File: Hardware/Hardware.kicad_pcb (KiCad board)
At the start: 2 copper layers, 60 x 40 mm, 52 parts, among them J1 Serial Wire Debug(SWD), J2 Conn_01x07 USART2, J3 Conn_01x07 LPUART1, J4 Conn_01x08 SPI1, J5 Conn_01x05 I2C, Q1 Q_NPN_BEC BSR17A, Q2 BC547, Q3 BC547, U1 Opamp_Quad, U4 TLV74115_SOT23-5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

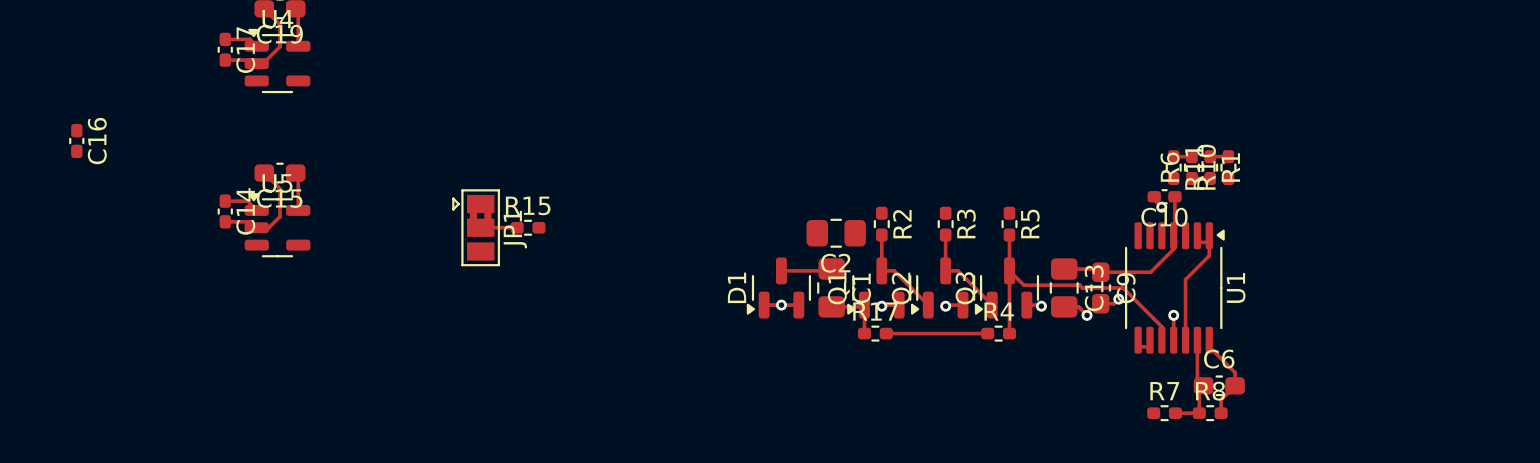
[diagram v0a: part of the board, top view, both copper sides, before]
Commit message: added more footprints and continued on the circuit diagram
- [ ] add antenna connection
- [ ] find suitable 390Mohm resistor
- [ ] add switches, reset and power
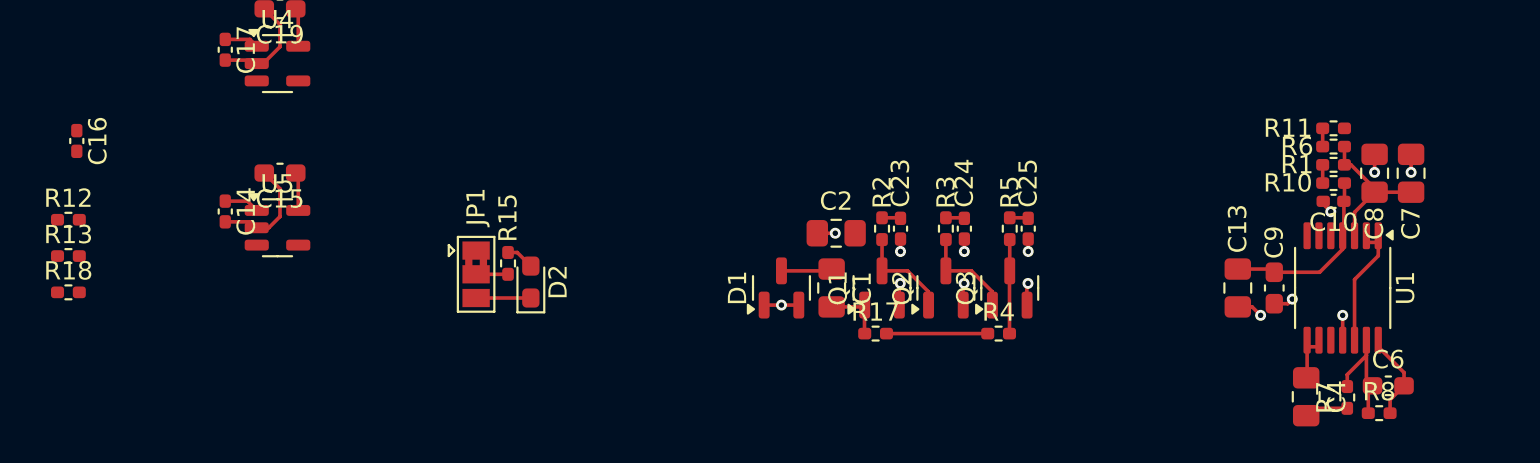
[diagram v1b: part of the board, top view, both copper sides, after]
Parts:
- added C23: 100nF, Capacitor_SMD:C_0402_1005Metric_Pad0.74x0.62mm_HandSolder, F.Cu at (61.8, 81.8)
- added C24: 100nF, Capacitor_SMD:C_0402_1005Metric_Pad0.74x0.62mm_HandSolder, F.Cu at (65.3, 81.8)
- added C25: 100nF, Capacitor_SMD:C_0402_1005Metric_Pad0.74x0.62mm_HandSolder, F.Cu at (68.8, 81.8)
- added C4: 1uF, Capacitor_SMD:C_0805_2012Metric_Pad1.18x1.45mm_HandSolder, F.Cu at (84.0, 91.0)
- added C7: 1uF, Capacitor_SMD:C_0805_2012Metric_Pad1.18x1.45mm_HandSolder, F.Cu at (89.8, 78.7)
- added C8: 1uF, Capacitor_SMD:C_0805_2012Metric_Pad1.18x1.45mm_HandSolder, F.Cu at (87.8, 78.7)
- added D2: LED BLUE, IF≈1mA@2.6V, APT1608LVBx, LED_SMD:LED_0603_1608Metric_Pad1.05x0.95mm_HandSolder, F.Cu at (41.5, 84.7)
- added R12: 2MΩ, Resistor_SMD:R_0402_1005Metric_Pad0.72x0.64mm_HandSolder, F.Cu at (16.2, 81.3)
- added R13: 39MΩ, Resistor_SMD:R_0402_1005Metric_Pad0.72x0.64mm_HandSolder, F.Cu at (16.2, 83.2)
- added R18: 2MΩ, Resistor_SMD:R_0402_1005Metric_Pad0.72x0.64mm_HandSolder, F.Cu at (16.2, 85.2)
- moved R7 10.0 mm to (86.2, 91.0), turned to 90 degrees
- moved C13 9.51 mm to (80.2, 85.0)
- moved C9 9.51 mm to (82.2, 85.0)
- moved C10 9.27 mm to (85.5, 80.2)
- moved C6 9.26 mm to (88.5, 90.4)
- moved R8 9.26 mm to (88.0, 91.9)
- moved U1 9.26 mm to (86.0, 85.0)
- moved R11 9.02 mm to (85.5, 76.2), turned to 0 degrees
- moved R6 7.85 mm to (85.5, 77.2), turned to 180 degrees
- moved R1 6.76 mm to (85.5, 78.2), turned to 0 degrees
- moved R10 5.82 mm to (85.5, 79.2), turned to 180 degrees
- moved JP1 2.56 mm to (38.5, 84.2)
- moved R15 2.24 mm to (40.2, 83.7), turned to 90 degrees
- moved R2 0.25 mm to (60.8, 81.8)
- moved R3 0.25 mm to (64.2, 81.8)
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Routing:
- net /Original Smog Detector/Output DC-Coupled: track 15.8 -> 5.15 mm
- net GND: track 24.8 -> 33.6 mm, vias 8 -> 14
- net Net-(U1A-+): track 1.00 -> 8.24 mm
- net +1V5: track 2.11 -> 5.18 mm
- net Net-(C4-Pad2): track 0.00 -> 2.42 mm
- net Net-(U1C--): track 0.65 -> 2.73 mm
- net Net-(D2-A): track 0.00 -> 1.56 mm
- net Net-(U1D--): track 5.18 -> 6.37 mm
- net +3V3: track 22.4 -> 22.9 mm

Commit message: PCB is done???
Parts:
- removed J3: Conn_01x07 LPUART1, Connector_PinHeader_2.54mm:PinHeader_1x07_P2.54mm_Vertical
- removed J4: Conn_01x08 SPI1, Connector_PinHeader_2.54mm:PinHeader_1x08_P2.54mm_Vertical
- removed J5: Conn_01x05 I2C, Connector_PinHeader_2.54mm:PinHeader_1x05_P2.54mm_Vertical
- removed JP10, JP2, JP3, JP4, JP5, JP6, JP7, JP8, JP9: SolderJumper_3_Open, Jumper:SolderJumper-3_P1.3mm_Open_Pad1.0x1.5mm
- added AE1: Antenna_Shield, Connector_PinHeader_2.54mm:PinHeader_1x02_P2.54mm_Vertical_SMD_Pin1Left, F.Cu at (74.8, 54.5)
- added C3: C_Polarized 10µF 16V, Capacitor_SMD:C_0805_2012Metric_Pad1.18x1.45mm_HandSolder, F.Cu at (61.9, 44.5)
- added C5: 150nF, Capacitor_SMD:C_0402_1005Metric_Pad0.74x0.62mm_HandSolder, F.Cu at (40.7, 31.2)
- added R14: 330MΩ preferably 390MΩ, Resistor_SMD:R_0603_1608Metric_Pad0.98x0.95mm_HandSolder, F.Cu at (31.2, 58.8)
- added SW1: Power_Hard, Button_Switch_SMD:SW_SPDT_PCM12, F.Cu at (22.3, 45.0)
- added SW2: Power_Soft, Button_Switch_SMD:SW_SPDT_PCM12, F.Cu at (22.3, 54.5)
- added SW3: Reset, Button_Switch_SMD:SW_Push_1P1T_NO_6x6mm_H9.5mm, F.Cu at (75.8, 26.0)
- J1: value Serial Wire Debug(SWD) -> SWD
- J2: footprint Connector_PinHeader_2.54mm:PinHeader_1x07_P2.54mm_Vertical -> Connector_PinHeader_2.54mm:PinHeader_1x07_P2.54mm_Vertical_SMD_Pin1Left
- moved J1 81.8 mm to (22.2, 22.2)
- moved C21 69.8 mm to (31.2, 34.2)
- moved J2 69.1 mm to (40.5, 39.8), turned to -90 degrees
- moved C18 63.8 mm to (32.5, 23.2), turned to 0 degrees
- moved C20 62.1 mm to (32.5, 24.8), turned to 0 degrees
- moved JP1 61.6 mm to (41.0, 22.8), turned to 0 degrees
- moved R8 60.9 mm to (68.9, 34.0), turned to 90 degrees
- moved C6 60.7 mm to (67.4, 33.5), turned to 90 degrees
- moved R15 59.2 mm to (40.4, 24.5), turned to 180 degrees
- moved D2 58.9 mm to (41.4, 25.8), turned to 180 degrees
- moved R7 58.2 mm to (68.0, 35.8), turned to 180 degrees
- moved C7 57.6 mm to (55.7, 32.2), turned to 180 degrees
- moved U6 57.1 mm to (32.5, 29.2), turned to 90 degrees
- moved C4 55.3 mm to (68.0, 38.0), turned to 0 degrees
- moved C8 54.8 mm to (55.7, 34.2), turned to 180 degrees
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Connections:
- J2 pad 2: /MCU/USART2_TX -> /MCU/PA2 A2
- J2 pad 3: /MCU/USART2_RX -> /MCU/PA3 A3
- J2 pad 4: /MCU/USART2_RTS -> /MCU/PA1 A1
- J2 pad 5: /MCU/USART2_CTS -> /MCU/PA0 A0
- J2 pad 6: /MCU/USART2_CK -> /MCU/PA4 A4
- R9 pad 2: /MCU/IN Signal -> /MCU/PA5 A5
- U1 pad 1: /MCU/IN Ref -> /MCU/PA6 A6
- U1 pad 12: /MCU/IN Ref -> /MCU/PA6 A6
- U1 pad 2: /MCU/IN Ref -> /MCU/PA6 A6
- U1 pad 5: unconnected-(U1B-+-Pad5) -> GND
- U1 pad 6: unconnected-(U1B---Pad6) -> +3V3
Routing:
- net +3V3: track 22.9 -> 104.6 mm
- net /MCU/NRST: track 0.00 -> 68.4 mm, vias 0 -> 4
- net /PSU/+BATT_SWITCH: track 3.82 -> 55.3 mm, vias 0 -> 6
- net /MCU/PA6 A6: track 0.00 -> 43.4 mm, vias 0 -> 2
- net /MCU/IN Ref: track 34.9 -> 0.00 mm, vias 3 -> 0
- net Net-(C6-Pad2): track 4.54 -> 34.4 mm
- net +1V5: track 5.18 -> 34.5 mm
- net /MCU/IN Signal: track 28.0 -> 0.00 mm, vias 3 -> 0
- net /Original Smog Detector/Output DC-Coupled: track 5.15 -> 28.3 mm
- net /PSU/EN: track 0.00 -> 19.4 mm
- net GND: track 33.6 -> 51.2 mm, vias 14 -> 30
- net /MCU/PA2 A2: track 0.00 -> 17.2 mm, vias 0 -> 2
- net /MCU/PA1 A1: track 0.00 -> 14.1 mm, vias 0 -> 2
- net /MCU/PA4 A4: track 0.00 -> 13.2 mm, vias 0 -> 2
- net /MCU/PA5 A5: track 0.00 -> 12.3 mm, vias 0 -> 2
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- added copper zone on B.Cu, net GND
- removed copper zone on F.Cu, net GND
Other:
- board text added: "+3V3"
- board text added: "Boot0"
- board text added: "GND"
- board text added: "NRST"
- board text added: "SWCLK"
- board text added: "SWDIO"

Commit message: added headphone jack footprint, SJ-3524-SMT
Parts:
- added C26: 10uF, Capacitor_SMD:C_0805_2012Metric_Pad1.18x1.45mm_HandSolder, F.Cu at (82.2, 46.5)
- added J6: AudioJack3_SwitchT, Connector_Audio:Jack_3.5mm_CUI_SJ-3524-SMT_Horizontal, F.Cu at (89.2, 39.7)
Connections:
- C6 pad 1: Net-(U1D--) -> Net-(U1D-+)
- C6 pad 2: Net-(C6-Pad2) -> Net-(U1B-+)
- R7 pad 2: Net-(U1D--) -> Net-(U1D-+)
- R8 pad 1: Net-(U1D--) -> Net-(U1D-+)
- R8 pad 2: Net-(C6-Pad2) -> Net-(U1B-+)
- R9 pad 1: Net-(C6-Pad2) -> Net-(U1B-+)
- U1 pad 12: /MCU/PA6 A6 -> Net-(U1D-+)
- U1 pad 13: Net-(U1D--) -> /MCU/PA6 A6
- U1 pad 14: Net-(C6-Pad2) -> Net-(U1B-+)
- U1 pad 5: GND -> Net-(U1B-+)
- U1 pad 6: +3V3 -> Net-(U1B--)
- U1 pad 7: unconnected-(U1-Pad7) -> Net-(U1B--)
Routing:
- net Net-(U1B-+): track 0.00 -> 34.4 mm
- net Net-(C6-Pad2): track 34.4 -> 0.00 mm
- net /MCU/PA6 A6: track 43.4 -> 49.7 mm
- net Net-(U1D--): track 6.37 -> 0.00 mm

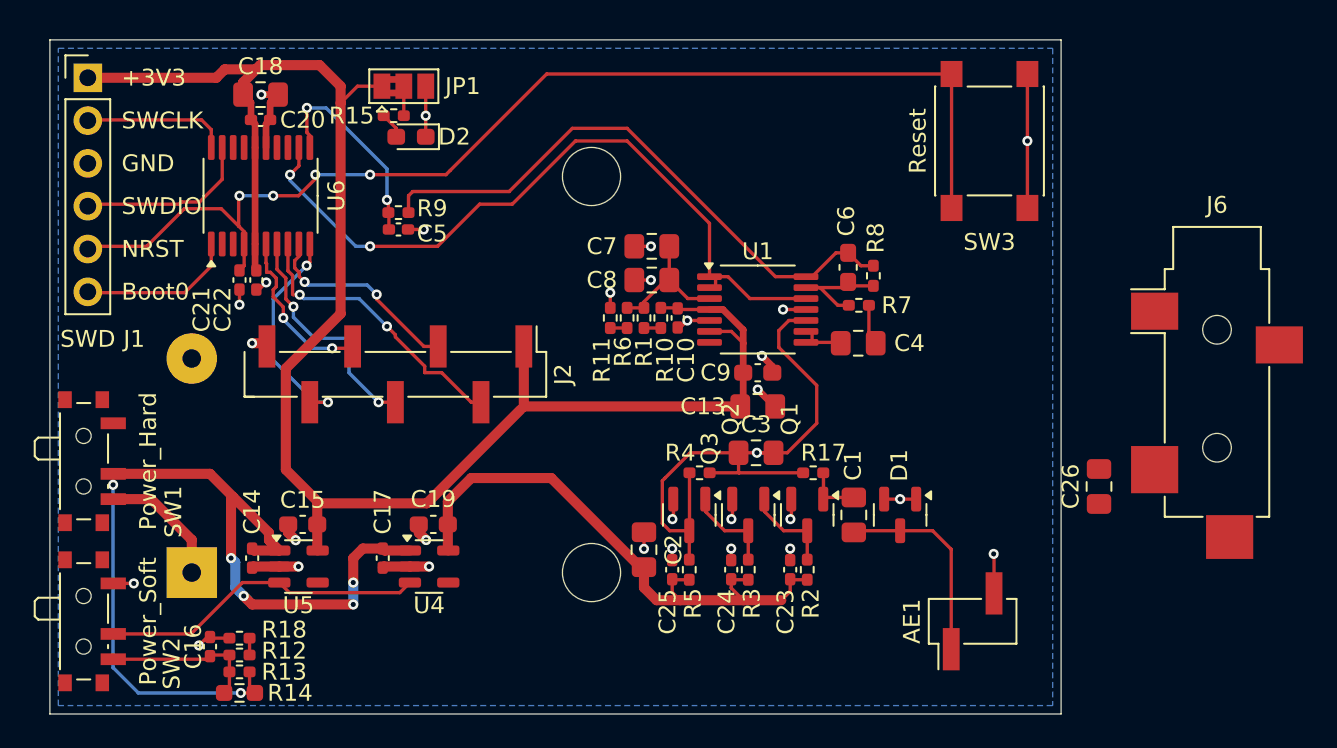
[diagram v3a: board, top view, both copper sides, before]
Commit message: PCB layed-out
- [x] headphone jack
- [x] UART header
- [x] Only one power trace with sub optimal return path
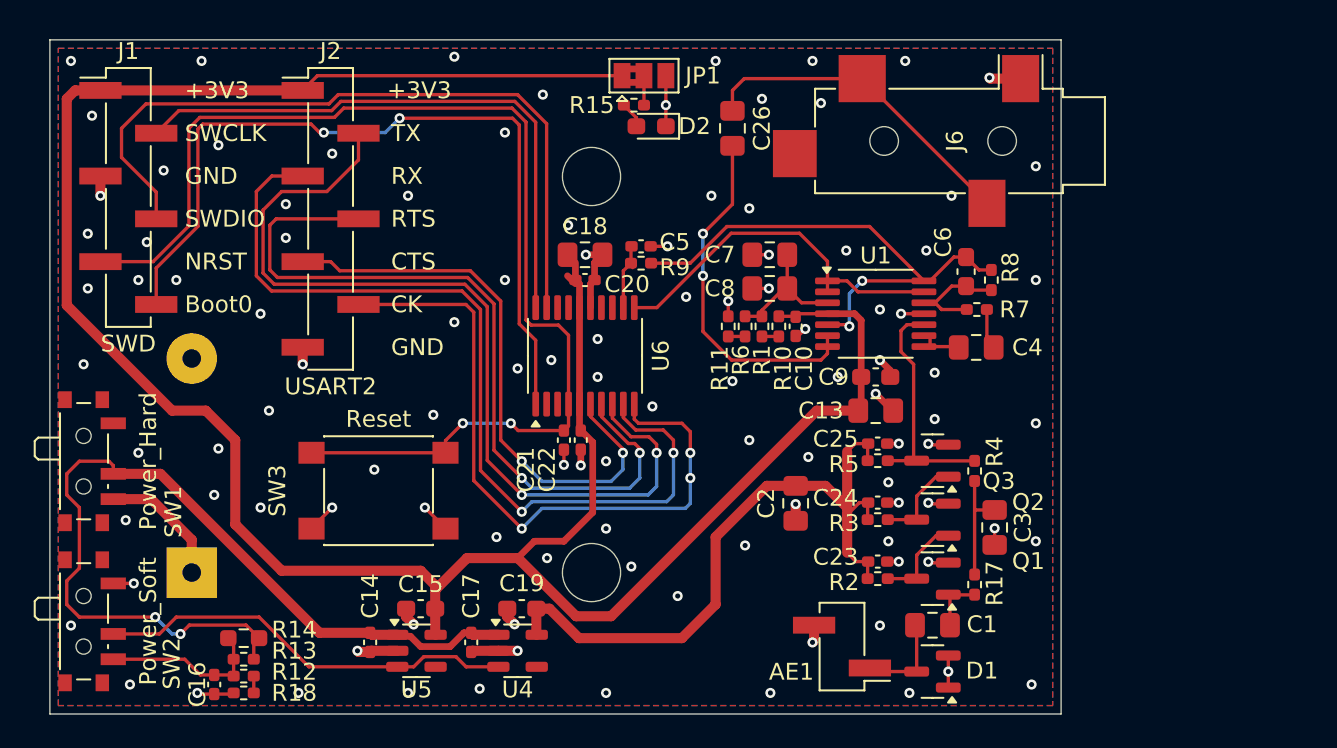
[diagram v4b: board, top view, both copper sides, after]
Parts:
- J1: footprint Connector_PinHeader_2.54mm:PinHeader_1x06_P2.54mm_Vertical -> Connector_PinHeader_2.54mm:PinHeader_1x06_P2.54mm_Vertical_SMD_Pin1Left
- J2: value Conn_01x07 USART2 -> USART2
- moved SW3 41.8 mm to (39.5, 46.8), turned to 180 degrees
- moved C26 30.4 mm to (60.5, 25.2)
- moved C18 21.5 mm to (51.8, 32.8)
- moved C20 21.5 mm to (51.8, 34.2)
- moved C21 21.5 mm to (50.5, 43.8)
- moved C22 21.5 mm to (51.5, 43.8)
- moved U6 21.5 mm to (51.8, 38.8)
- moved J6 20.5 mm to (74.0, 26.0), turned to -90 degrees
- moved R4 16.3 mm to (74.9, 45.6), turned to 90 degrees
- moved C3 14.8 mm to (76.1, 48.9), turned to -90 degrees
- moved Q3 14.8 mm to (72.4, 45.0), turned to 180 degrees
- moved R9 14.7 mm to (55.1, 33.2)
- moved C5 14.4 mm to (55.1, 32.2)
- moved C25 14.3 mm to (69.1, 44.0), turned to 0 degrees
- moved D2 14.3 mm to (55.7, 25.1)
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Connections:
- C5 pad 1: /MCU/PA5 A5 -> /MCU/PA6 A6
- R9 pad 2: /MCU/PA5 A5 -> /MCU/PA6 A6
- U1 pad 1: /MCU/PA6 A6 -> /MCU/PA5 A5
- U1 pad 13: /MCU/PA6 A6 -> /MCU/PA5 A5
- U1 pad 2: /MCU/PA6 A6 -> /MCU/PA5 A5
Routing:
- net /MCU/PA6 A6: track 49.7 -> 3.88 mm, vias 2 -> 0
- net +3V3: track 104.6 -> 145.2 mm
- net /MCU/PA3 A3: track 12.3 -> 52.3 mm
- net /MCU/PB9 Boot0: track 9.31 -> 48.3 mm, vias 0 -> 2
- net /MCU/PA2 A2: track 17.2 -> 53.2 mm
- net /MCU/PA13 SWDIO: track 10.5 -> 43.9 mm
- net /MCU/PA1 A1: track 14.1 -> 46.3 mm
- net /MCU/PA4 A4: track 13.2 -> 40.4 mm, vias 2 -> 3
- net /MCU/PA14 SWCLK: track 8.64 -> 34.8 mm
- net /MCU/PA0 A0: track 10.1 -> 34.2 mm
- net Net-(U1B--): track 0.00 -> 21.1 mm, vias 0 -> 2
- net Net-(C26-Pad2): track 0.00 -> 19.7 mm
- net /Original Smog Detector/Output DC-Coupled: track 28.3 -> 14.8 mm
- net /MCU/PA5 A5: track 12.3 -> 21.8 mm, vias 2 -> 0
- net Net-(U1D-+): track 0.00 -> 6.57 mm
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- added copper zone on F.Cu, net GND
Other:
- board text added: "CK"
- board text added: "CTS"
- board text added: "RTS"
- board text added: "RX"
- board text added: "TX"

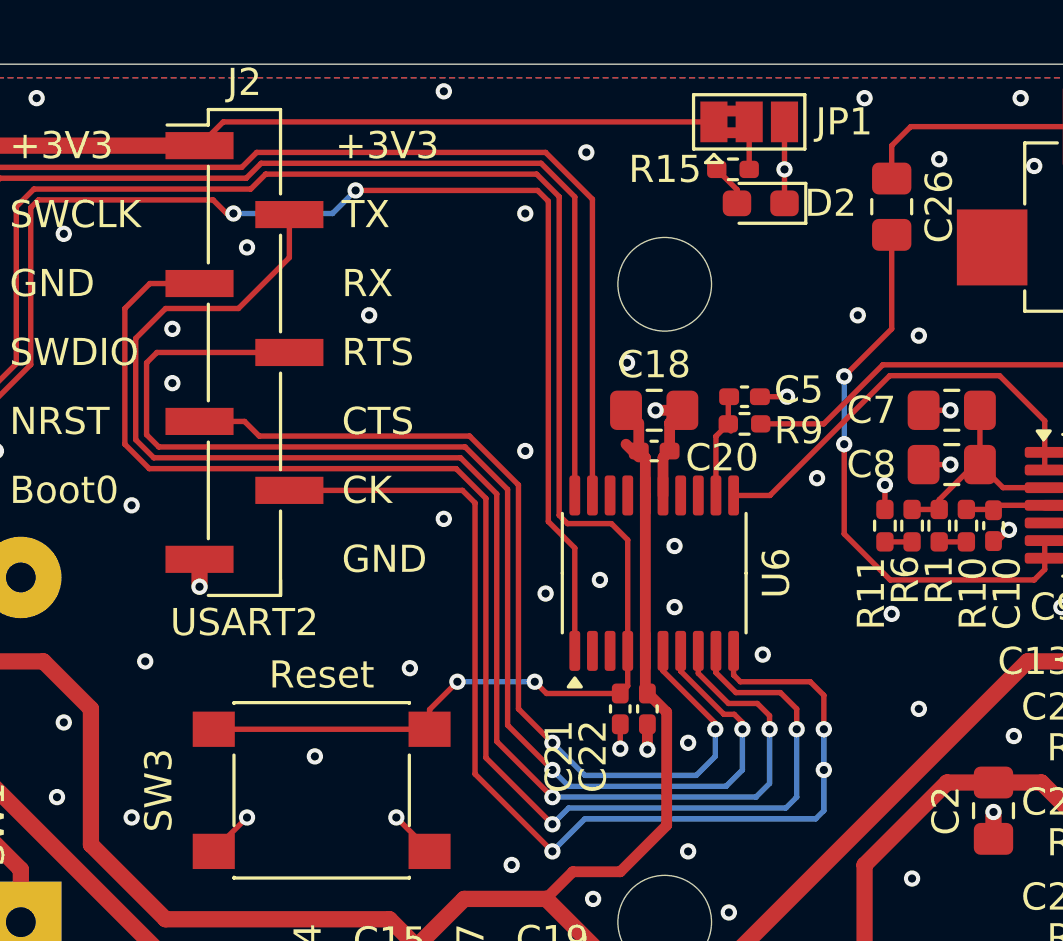
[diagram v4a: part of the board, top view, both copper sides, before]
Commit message: added four leds
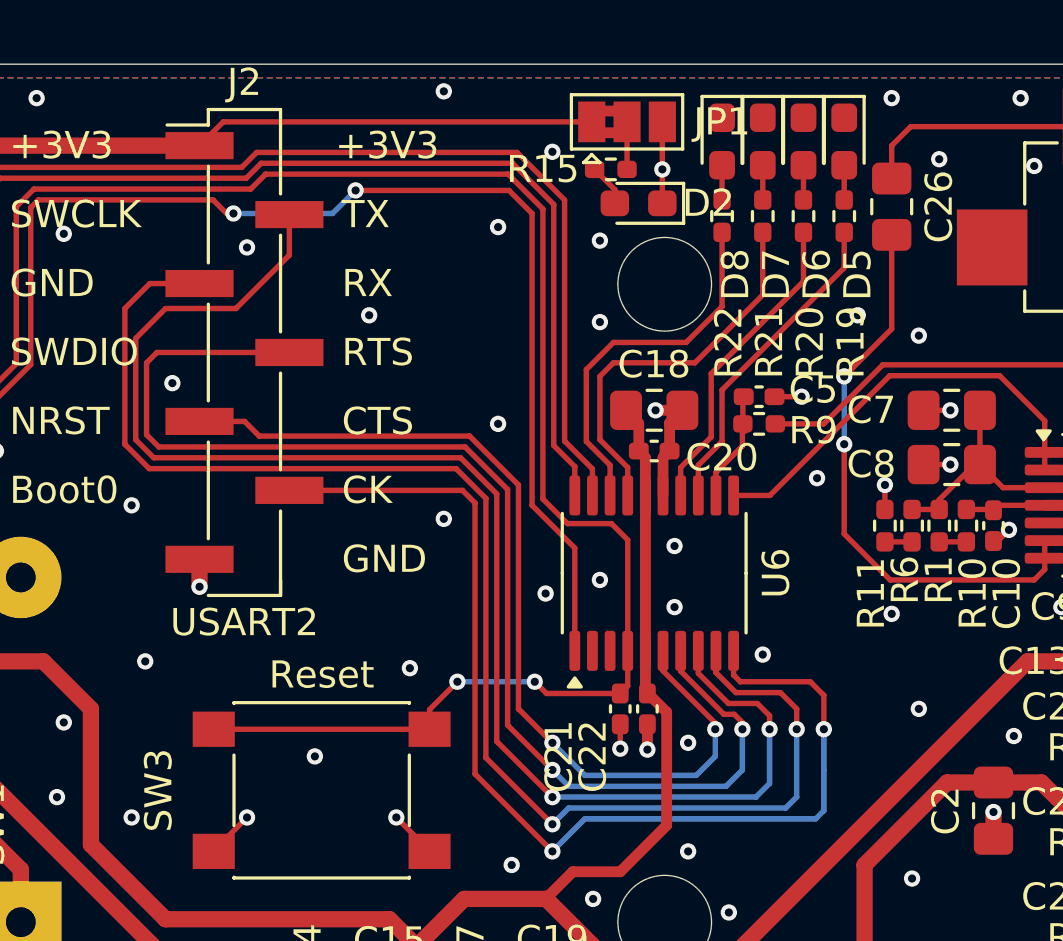
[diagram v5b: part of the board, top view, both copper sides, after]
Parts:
- added D5: LED RED, APT1608LSECK/J3-PRV, LED_SMD:LED_0603_1608Metric_Pad1.05x0.95mm_HandSolder, F.Cu at (58.8, 22.8)
- added D6: LED ORANGE, APT1608LSECK/J4-PRV, LED_SMD:LED_0603_1608Metric_Pad1.05x0.95mm_HandSolder, F.Cu at (57.2, 22.8)
- added D7: LED YELLOW, APT1608LSYCK/J3-PRV, LED_SMD:LED_0603_1608Metric_Pad1.05x0.95mm_HandSolder, F.Cu at (55.8, 22.8)
- added D8: LED GREEN, APT1608LZGCK, LED_SMD:LED_0603_1608Metric_Pad1.05x0.95mm_HandSolder, F.Cu at (54.2, 22.8)
- added R19: 820Ω, Resistor_SMD:R_0402_1005Metric_Pad0.72x0.64mm_HandSolder, F.Cu at (58.8, 25.6)
- added R20: 820Ω, Resistor_SMD:R_0402_1005Metric_Pad0.72x0.64mm_HandSolder, F.Cu at (57.2, 25.6)
- added R21: 820Ω, Resistor_SMD:R_0402_1005Metric_Pad0.72x0.64mm_HandSolder, F.Cu at (55.8, 25.6)
- added R22: 330Ω, Resistor_SMD:R_0402_1005Metric_Pad0.72x0.64mm_HandSolder, F.Cu at (54.2, 25.6)
- moved D2 4.50 mm to (51.2, 25.1)
- moved JP1 4.50 mm to (50.8, 22.1)
- moved R15 4.50 mm to (50.2, 23.9)
- moved C5 0.54 mm to (55.6, 32.2)
- moved R9 0.54 mm to (55.6, 33.2)
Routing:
- net /MCU/PA9: track 0.00 -> 14.4 mm
- net /MCU/PA10: track 0.00 -> 13.7 mm
- net /MCU/PA7 A7: track 0.00 -> 11.9 mm
- net /MCU/PB1 A9 VREF_OUT: track 0.00 -> 11.6 mm
- net +3V3: track 145.2 -> 140.0 mm
- net Net-(D8-A): track 0.00 -> 1.28 mm
- net Net-(D7-A): track 0.00 -> 1.28 mm
- net Net-(D6-A): track 0.00 -> 1.28 mm
- net Net-(D5-A): track 0.00 -> 1.28 mm
- net /MCU/PA14 SWCLK: track 34.8 -> 34.2 mm
- net /MCU/PA13 SWDIO: track 43.9 -> 43.3 mm
- net /MCU/PB9 Boot0: track 48.3 -> 47.7 mm
- net /MCU/NRST: track 69.5 -> 68.9 mm
- net Net-(U1B-+): track 31.0 -> 30.4 mm
- net /MCU/PA4 A4: vias 3 -> 2
